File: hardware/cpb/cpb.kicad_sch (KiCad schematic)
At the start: 132 parts, among them J1 Spacecraft Bus Stacking Conne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, J10 SW1, J11 SW2, J12 SW3, J13 PISW1, J14 μSW1, J15 μSW2, J16 μSW3, J17 μSW4, J2 I2CExt, J3 DAC1BUF, J4 DAC2BUF, J6 Raspberry Pi Zero 2W, J7 ADC6/7, J8 ADC2/3, J9 4FBRG, J99 RBFJUMP, Q1 PMBT2222A, Q2 IRF9393, Q3 MBT2222ADW1T1, Q4 PMBT2222A, U1 TS912, U2 ADR420ARMZ, U3 KF33BDT, U4 STM32L072R_B-Z_Tx, U5 AP62301WU, U6 SC16IS750xBS, Y1 14.7456MHz

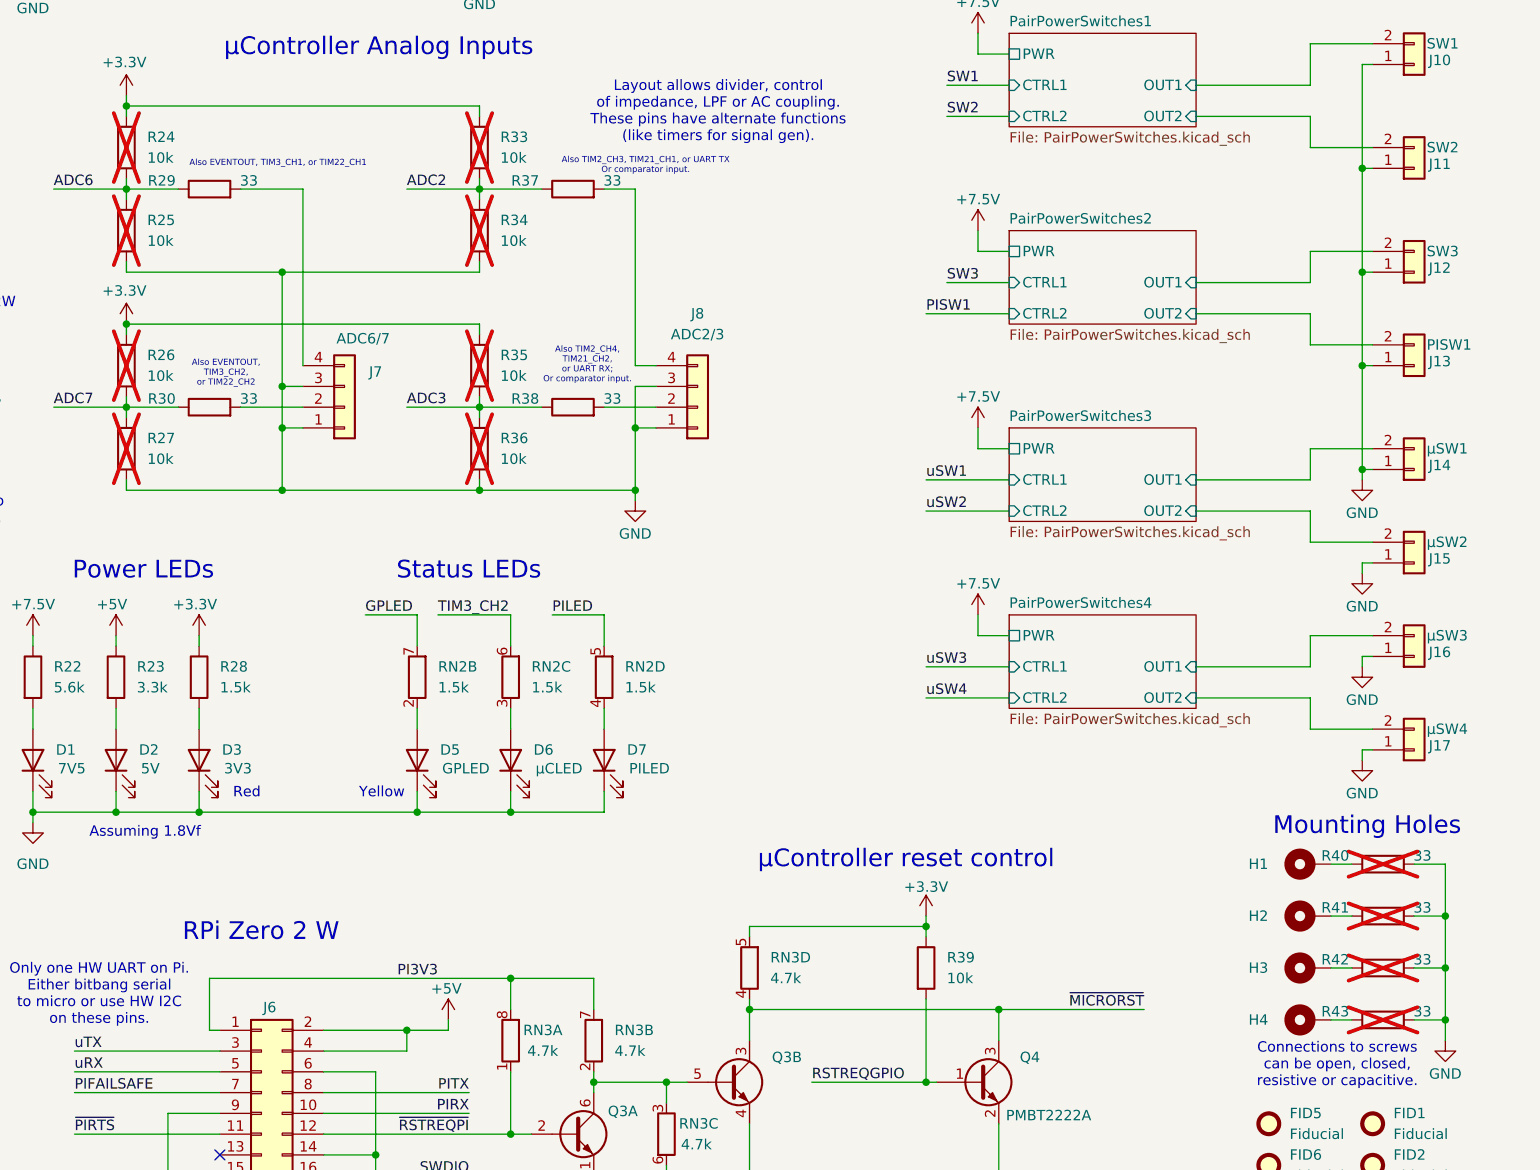
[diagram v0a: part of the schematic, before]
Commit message: cpb: property updates, part numbers
RN2 part number was wrong.

Set DNP components value to "DNP" to aid ordering.
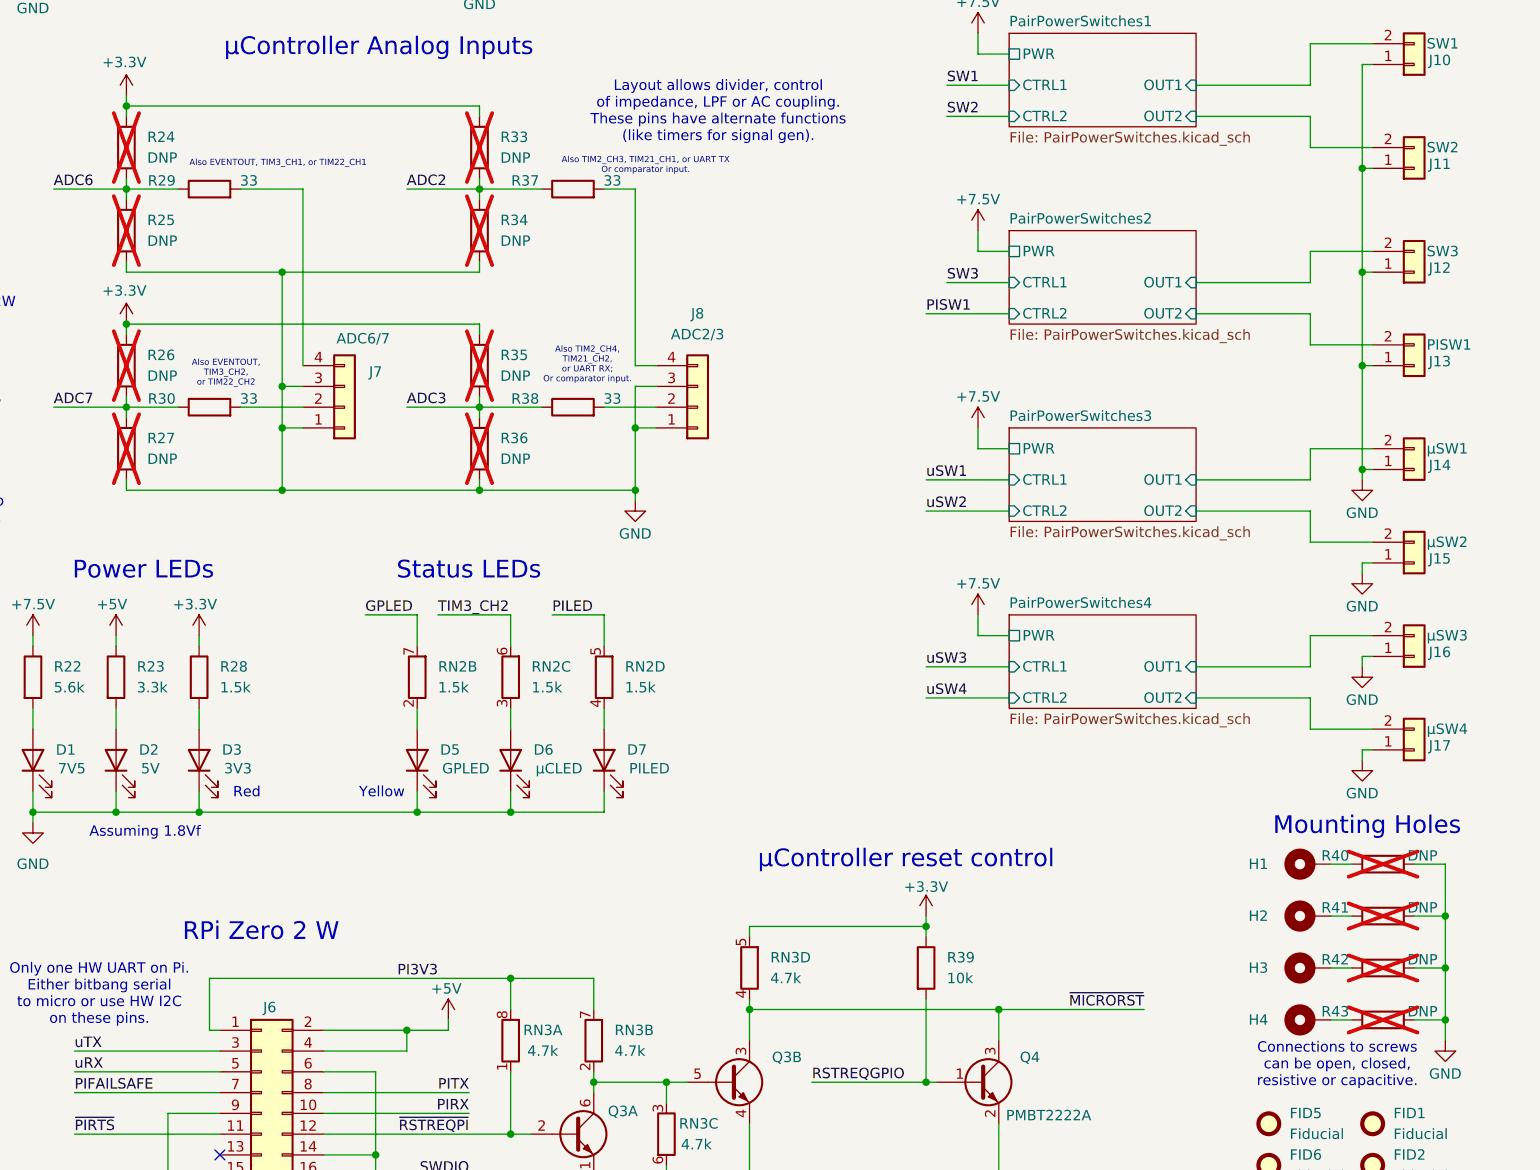
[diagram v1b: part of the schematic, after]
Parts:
- R24, R25, R26, R27, R33, R34, R35, R36: value 10k -> DNP
- R40, R41, R42, R43: value 33 -> DNP
- RN2: LCSC C110924 -> C723702
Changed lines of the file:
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@@
 			)
 		)
-		(property "Value" "10k"
+		(property "Value" "DNP"
 			(at 298.45 99.0599 0)
 			(effects
@@
 			)
 		)
-		(property "Value" "33"
+		(property "Value" "DNP"
 			(at 411.226 197.104 90)
 			(effects
@@
 			)
 		)
-		(property "Value" "33"
+		(property "Value" "DNP"
 			(at 411.226 190.754 90)
 			(effects
@@
 			)
 		)
-		(property "Value" "10k"
+		(property "Value" "DNP"
 			(at 255.27 99.0599 0)
 			(effects
@@
 			)
 		)
-		(property "Value" "10k"
+		(property "Value" "DNP"
 			(at 255.27 109.2199 0)
 			(effects
@@
 			)
 		)
-		(property "Value" "10k"
+		(property "Value" "DNP"
 			(at 255.27 125.7299 0)
 			(effects
@@
 			)
 		)
-		(property "LCSC" "C110924"
+		(property "LCSC" "C723702"
 			(at 288.29 162.56 0)
 			(effects
@@
 			)
 		)
-		(property "Value" "33"
+		(property "Value" "DNP"
 			(at 411.226 184.404 90)
 			(effects
@@
 			)
 		)
-		(property "LCSC" "C110924"
+		(property "LCSC" "C723702"
 			(at 311.15 162.56 0)
 			(effects
@@
 			)
 		)
-		(property "Value" "10k"
+		(property "Value" "DNP"
 			(at 298.45 135.8899 0)
 			(effects
@@
 			)
 		)
-		(property "Value" "10k"
+		(property "Value" "DNP"
 			(at 298.45 125.7299 0)
 			(effects
@@
 			)
 		)
-		(property "LCSC" "C110924"
+		(property "LCSC" "C723702"
 			(at 299.72 162.56 0)
 			(effects
@@
 			)
 		)
-		(property "Value" "10k"
+		(property "Value" "DNP"
 			(at 255.27 135.8899 0)
 			(effects
@@
 			)
 		)
-		(property "Value" "33"
+		(property "Value" "DNP"
 			(at 411.226 203.454 90)
 			(effects
@@
 			)
 		)
-		(property "Value" "10k"
+		(property "Value" "DNP"
 			(at 298.45 109.2199 0)
 			(effects

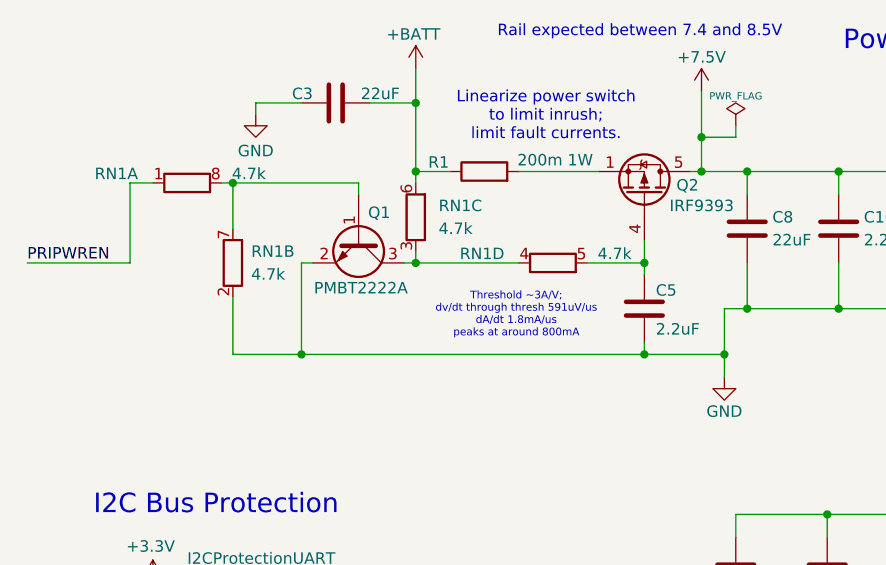
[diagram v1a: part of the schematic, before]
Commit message: hardware/cpb: RN vias and 2.2 nF capacitor fixed.
Vias on all RNs are now have a proper fanout and C37 was moved and now connects between the gate and VBATT+.
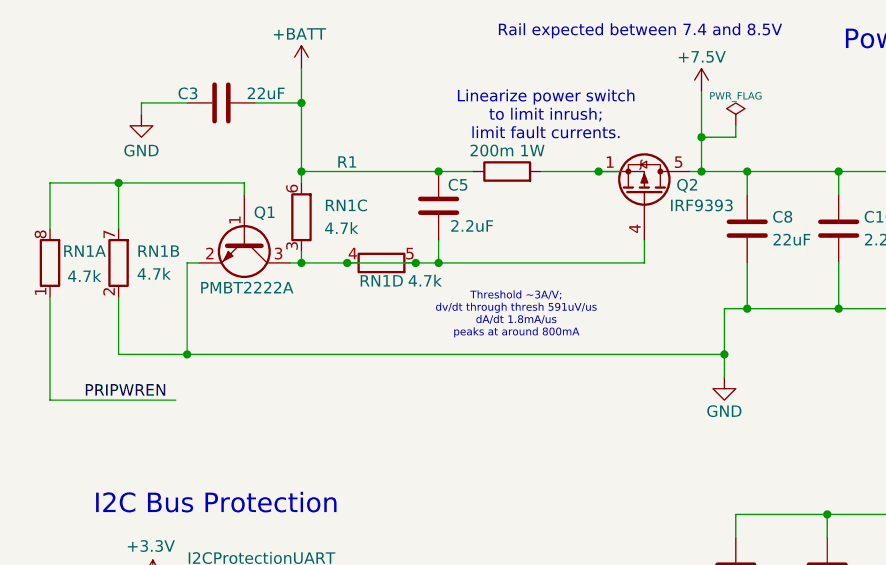
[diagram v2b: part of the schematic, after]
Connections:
- net +BATT: now also C5.1
- net GND: no longer C5.2
- net at Q2.4 (G), RN1.5 (R4.2): now also C5.2, Q1.3 (C), RN1.3 (R3.1), RN1.4 (R4.1); no longer C5.1
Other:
- moved on the sheet: C3, C5, Q1, R1, RN1A, RN1B, RN1C, RN1D

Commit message: hardware/cpb: changed from european to american symbols.
RN parts still are european for now. Changed via TextEdit replace all tool. Device:R --> Device:R_US
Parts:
- R1, R10, R11, R12, R13, R14, R15, R16, R17, R18, R19, R2, R20, R21, R22, R23, R24, R25, R26, R27, R28, R29, R3, R30, R31, R32, R33, R34, R35, R36, R37, R38, R39, R4, R40, R41, R42, R43, R44, R45, R5, R6, R7, R8, R9: symbol Device:R -> Device:R_US
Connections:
- net at C5.2, Q2.4 (G), RN1.5 (R4.2): no longer Q1.3 (C), RN1.3 (R3.1), RN1.4 (R4.1)
- new net: Q1.3 (C), RN1.3 (R3.1), RN1.4 (R4.1)
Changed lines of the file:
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@@
 	)
 	(junction
-		(at 49.53 39.37)
-		(diameter 0)
-		(color 0 0 0 0)
-	)
-	(junction
 		(at 226.06 213.36)
 		(diameter 0)
@@
 	)
 	(junction
-		(at 57.15 39.37)
-		(diameter 0)
-		(color 0 0 0 0)
-	)
-	(junction
 		(at 152.4 29.21)
 		(diameter 0)
@@
 	(wire
 		(pts
-			(xy 49.53 39.37) (xy 57.15 39.37)
-		)
-		(stroke
-			(width 0)
-			(type default)
-		)
-	)
-	(wire
-		(pts
 			(xy 171.45 238.76) (xy 171.45 247.65)
 		)
@@
 	)
 	(symbol
-		(lib_id "Device:R")
+		(lib_id "Device:R_US")
 		(at 222.25 34.29 90)
 		(unit 1)
@@
 	)
 	(symbol
-		(lib_id "Device:R")
+		(lib_id "Device:R_US")
 		(at 271.78 27.94 90)
 		(unit 1)
@@
 	)
 	(symbol
-		(lib_id "Device:R")
+		(lib_id "Device:R_US")
 		(at 95.25 243.84 90)
 		(unit 1)
@@
 	)
 	(symbol
-		(lib_id "Device:R")
+		(lib_id "Device:R_US")
 		(at 295.91 97.79 0)
 		(unit 1)
@@
 	)
 	(symbol
-		(lib_id "Device:R")
+		(lib_id "Device:R_US")
 		(at 163.83 125.73 90)
 		(unit 1)
@@
 	)
 	(symbol
-		(lib_id "Device:R")
+		(lib_id "Device:R_US")
 		(at 406.4 198.12 90)
 		(unit 1)
@@
 	)
 	(symbol
-		(lib_id "Device:R")
+		(lib_id "Device:R_US")
 		(at 241.3 162.56 0)
 		(unit 1)
@@
 	)
 	(symbol
-		(lib_id "Device:R")
+		(lib_id "Device:R_US")
 		(at 406.4 191.77 90)
 		(unit 1)
@@
 	)
 	(symbol
-		(lib_id "Device:R")
+		(lib_id "Device:R_US")
 		(at 307.34 102.87 90)
 		(unit 1)
@@
 	)
 	(symbol
-		(lib_id "Device:R")
+		(lib_id "Device:R_US")
 		(at 134.62 207.01 90)
 		(unit 1)
@@
 	)
 	(symbol
-		(lib_id "Device:R")
+		(lib_id "Device:R_US")
 		(at 307.34 129.54 90)
 		(unit 1)
@@
 	)
 	(symbol
-		(lib_id "Device:R")
+		(lib_id "Device:R_US")
 		(at 261.62 162.56 0)
 		(unit 1)
@@
 	)
 	(symbol
-		(lib_id "Device:R")
+		(lib_id "Device:R_US")
 		(at 252.73 97.79 0)
 		(unit 1)
@@
 	)
 	(symbol
-		(lib_id "Device:R")
+		(lib_id "Device:R_US")
 		(at 262.89 129.54 90)
 		(unit 1)
@@
 	)
 	(symbol
-		(lib_id "Device:R")
+		(lib_id "Device:R_US")
 		(at 134.62 217.17 90)
 		(unit 1)
@@
 	)
 	(symbol
-		(lib_id "Device:R")
+		(lib_id "Device:R_US")
 		(at 74.93 243.84 90)
 		(unit 1)
@@
 	)
 	(symbol
-		(lib_id "Device:R")
+		(lib_id "Device:R_US")
 		(at 350.52 198.12 0)
 		(unit 1)
@@
 	)
 	(symbol
-		(lib_id "Device:R")
+		(lib_id "Device:R_US")
 		(at 252.73 107.95 0)
 		(unit 1)
@@
 	)
 	(symbol
-		(lib_id "Device:R")
+		(lib_id "Device:R_US")
 		(at 292.1 231.14 90)
 		(unit 1)
@@
 	)
 	(symbol
-		(lib_id "Device:R")
+		(lib_id "Device:R_US")
 		(at 252.73 124.46 0)
 		(unit 1)
@@
 	)
 	(symbol
-		(lib_id "Device:R")
+		(lib_id "Device:R_US")
 		(at 224.79 135.89 90)
 		(unit 1)
@@
 	)
 	(symbol
-		(lib_id "Device:R")
+		(lib_id "Device:R_US")
 		(at 95.25 200.66 90)
 		(unit 1)
@@
 	)
 	(symbol
-		(lib_id "Device:R")
+		(lib_id "Device:R_US")
 		(at 153.67 209.55 90)
 		(unit 1)
@@
 	)
 	(symbol
-		(lib_id "Device:R")
+		(lib_id "Device:R_US")
 		(at 146.05 99.06 0)
 		(mirror y)
@@
 	)
 	(symbol
-		(lib_id "Device:R")
+		(lib_id "Device:R_US")
 		(at 406.4 185.42 90)
 		(unit 1)
@@
 	)
 	(symbol
-		(lib_id "Device:R")
+		(lib_id "Device:R_US")
 		(at 134.62 238.76 90)
 		(unit 1)
@@
 	)
 	(symbol
-		(lib_id "Device:R")
+		(lib_id "Device:R_US")
 		(at 74.93 212.09 90)
 		(unit 1)
@@
 	)
 	(symbol
-		(lib_id "Device:R")
+		(lib_id "Device:R_US")
 		(at 262.89 102.87 90)
 		(unit 1)
@@
 	)
 	(symbol
-		(lib_id "Device:R")
+		(lib_id "Device:R_US")
 		(at 134.62 248.92 90)
 		(unit 1)
@@
 	)
 	(symbol
-		(lib_id "Device:R")
+		(lib_id "Device:R_US")
 		(at 194.31 39.37 0)
 		(unit 1)
@@
 	)
 	(symbol
-		(lib_id "Device:R")
+		(lib_id "Device:R_US")
 		(at 153.67 238.76 90)
 		(unit 1)
@@
 	)
 	(symbol
-		(lib_id "Device:R")
+		(lib_id "Device:R_US")
 		(at 251.46 162.56 0)
 		(unit 1)
@@
 	)
 	(symbol
-		(lib_id "Device:R")
+		(lib_id "Device:R_US")
 		(at 217.17 39.37 0)
 		(unit 1)
@@
 	)
 	(symbol
-		(lib_id "Device:R")
+		(lib_id "Device:R_US")
 		(at 295.91 134.62 0)
 		(unit 1)
@@
 	)
 	(symbol
-		(lib_id "Device:R")
+		(lib_id "Device:R_US")
 		(at 165.1 107.95 90)
 		(unit 1)
@@
 	)
 	(symbol
-		(lib_id "Device:R")
+		(lib_id "Device:R_US")
 		(at 295.91 124.46 0)
 		(unit 1)
@@
 	)
 	(symbol
-		(lib_id "Device:R")
+		(lib_id "Device:R_US")
 		(at 95.25 231.14 90)
 		(unit 1)
@@
 	)
 	(symbol
-		(lib_id "Device:R")
+		(lib_id "Device:R_US")
 		(at 134.62 222.25 90)
 		(unit 1)
@@
 	)
 	(symbol
-		(lib_id "Device:R")
+		(lib_id "Device:R_US")
 		(at 67.31 29.21 90)
 		(unit 1)
@@
 	)
 	(symbol
-		(lib_id "Device:R")
+		(lib_id "Device:R_US")
 		(at 252.73 134.62 0)
 		(unit 1)
@@
 	)
 	(symbol
-		(lib_id "Device:R")
+		(lib_id "Device:R_US")
 		(at 95.25 212.09 90)
 		(unit 1)
@@
 	)
 	(symbol
-		(lib_id "Device:R")
+		(lib_id "Device:R_US")
 		(at 134.62 252.73 90)
 		(unit 1)
@@
 	)
 	(symbol
-		(lib_id "Device:R")
+		(lib_id "Device:R_US")
 		(at 406.4 204.47 90)
 		(unit 1)
@@
 	)
 	(symbol
-		(lib_id "Device:R")
+		(lib_id "Device:R_US")
 		(at 295.91 107.95 0)
 		(unit 1)
@@
 	)
 	(symbol
-		(lib_id "Device:R")
+		(lib_id "Device:R_US")
 		(at 224.79 138.43 90)
 		(unit 1)
